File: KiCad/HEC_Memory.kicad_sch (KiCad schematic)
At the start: 10 parts, among them U13 74LS245, U14 74LS245, U15 74LS32, U16 74LS32, U2 AS6C4008-55PCN, U22 74LS02, U3 AS6C4008-55PCN, U4 CY7C199, U5 CY7C199, U9 74LS574

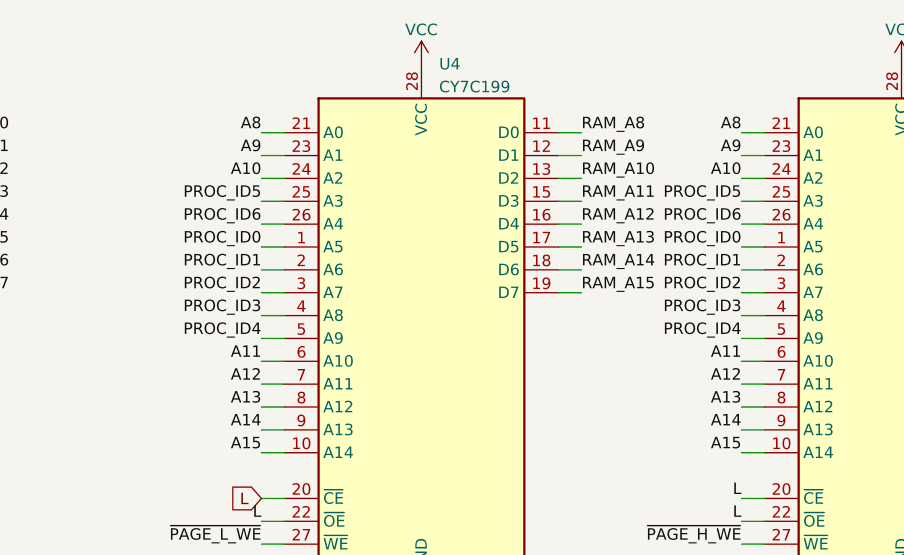
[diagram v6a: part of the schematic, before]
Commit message: More routing
Even more routing... Maybe 50% finished? The remaining 50% is probably harder though.
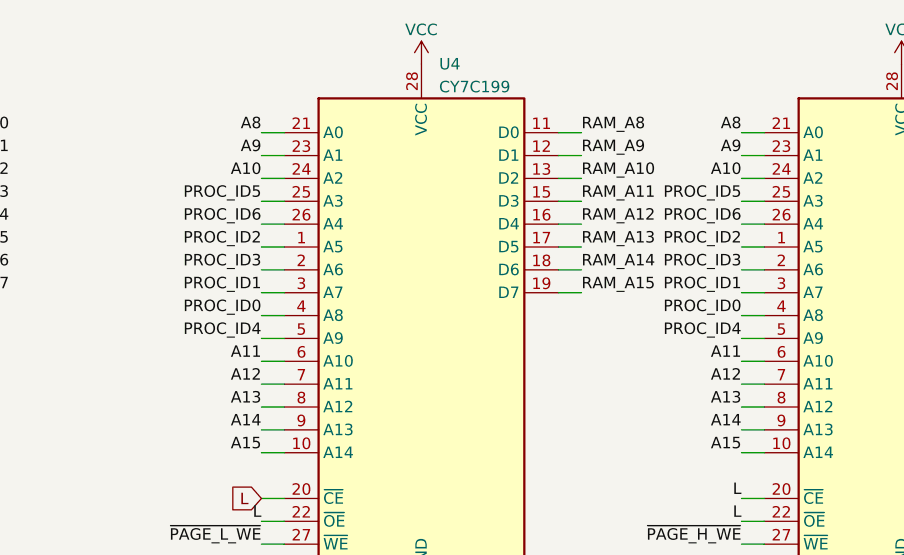
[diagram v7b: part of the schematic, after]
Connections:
- net PROC_ID0: now also U4.4 (A8), U5.4 (A8); no longer U4.1 (A5), U5.1 (A5)
- net PROC_ID1: now also U4.3 (A7), U5.3 (A7); no longer U4.2 (A6), U5.2 (A6)
- net PROC_ID2: now also U4.1 (A5), U5.1 (A5); no longer U4.3 (A7), U5.3 (A7)
- net PROC_ID3: now also U4.2 (A6), U5.2 (A6); no longer U4.4 (A8), U5.4 (A8)

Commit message: Livestream commit
Committing live! Just to make sure that I don't lose 1 day of work.
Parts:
- added U41: 74LS02, Package_DIP:DIP-14_W7.62mm_Socket, symbol 74xx:74LS02
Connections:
- net GND: now also U41.8
- net RAM_A19: now also U41.9; no longer U22.2, U22.3
- net VCC: now also U22.2, U22.3
- net ~{RAM_A19}: now also U41.10; no longer U22.1
- no-connect marks 0 -> 1
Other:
- moved on the sheet: U22A
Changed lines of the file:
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@@
 (kicad_sch (version 20230121) (generator eeschema)
   (paper "A4")
-  (junction (at 104.14 87.63) (diameter 0) (color 0 0 0 0)
-  )
+  (junction (at 69.215 86.36) (diameter 0) (color 0 0 0 0)
+  )
+  (no_connect (at 84.455 88.9))
   (wire (pts (xy 269.24 35.56) (xy 271.78 35.56))
     (stroke (width 0) (type default))
@@
     (stroke (width 0) (type default))
   )
-  (wire (pts (xy 104.14 85.09) (xy 104.14 87.63))
-    (stroke (width 0) (type default))
-  )
   (wire (pts (xy 269.875 33.02) (xy 269.24 33.02))
     (stroke (width 0) (type default))
@@
     (stroke (width 0) (type default))
   )
+  (wire (pts (xy 69.215 86.36) (xy 69.215 91.44))
+    (stroke (width 0) (type default))
+  )
   (wire (pts (xy 168.91 107.95) (xy 171.45 107.95))
     (stroke (width 0) (type default))
@@
     (stroke (width 0) (type default))
   )
+  (wire (pts (xy 92.075 85.09) (xy 104.14 85.09))
+    (stroke (width 0) (type default))
+  )
   (wire (pts (xy 190.5 158.115) (xy 190.5 148.59))
     (stroke (width 0) (type default))
@@
     (stroke (width 0) (type default))
   )
-  (wire (pts (xy 104.14 87.63) (xy 104.14 90.17))
-    (stroke (width 0) (type default))
-  )
   (wire (pts (xy 218.44 38.1) (xy 215.9 38.1))
     (stroke (width 0) (type default))
@@
     (stroke (width 0) (type default))
   )
+  (wire (pts (xy 69.215 82.55) (xy 69.215 86.36))
+    (stroke (width 0) (type default))
+  )
   (wire (pts (xy 50.8 167.64) (xy 53.34 167.64))
     (stroke (width 0) (type default))
@@
     (stroke (width 0) (type default))
   )
+  (wire (pts (xy 92.075 85.09) (xy 92.075 93.98))
+    (stroke (width 0) (type default))
+  )
   (wire (pts (xy 168.91 93.98) (xy 171.45 93.98))
     (stroke (width 0) (type default))
@@
     (stroke (width 0) (type default))
   )
-  (wire (pts (xy 101.6 87.63) (xy 104.14 87.63))
+  (wire (pts (xy 101.6 90.17) (xy 104.14 90.17))
     (stroke (width 0) (type default))
   )
@@
     (effects (font (size 1.27 1.27)) (justify left bottom))
   )
-  (label "RAM_A19" (at 101.6 87.63 180) (fields_autoplaced)
+  (label "RAM_A19" (at 101.6 90.17 180) (fields_autoplaced)
     (effects (font (size 1.27 1.27)) (justify right bottom))
   )
@@
         (path "/87935374-b60a-4f41-99da-94b76103dd77/933a6f90-eb98-4eb1-8c19-8a76228aece1"
           (reference "#PWR011") (unit 1)
+        )
+      )
+    )
+  )
+  (symbol (lib_id "power:VCC") (at 69.215 82.55 0) (unit 1)
+    (in_bom yes) (on_board yes) (dnp no) (fields_autoplaced)
+    (property "Reference" "#PWR0107" (at 69.215 86.36 0)
+      (effects (font (size 1.27 1.27)) hide)
+    )
+    (property "Value" "VCC" (at 69.215 79.375 0)
+      (effects (font (size 1.27 1.27)))
+    )
+    (property "Footprint" "" (at 69.215 82.55 0)
+      (effects (font (size 1.27 1.27)) hide)
+    )
+    (property "Datasheet" "" (at 69.215 82.55 0)
+      (effects (font (size 1.27 1.27)) hide)
+    )
+    (pin "1")
+    (instances
+      (project "HEC1"
+        (path "/87935374-b60a-4f41-99da-94b76103dd77/933a6f90-eb98-4eb1-8c19-8a76228aece1"
+          (reference "#PWR0107") (unit 1)
         )
       )
@@
     )
   )
+  (symbol (lib_id "power:GND") (at 92.075 93.98 0) (unit 1)
+    (in_bom yes) (on_board yes) (dnp no)
+    (property "Reference" "#PWR0107" (at 92.075 100.33 0)
+      (effects (font (size 1.27 1.27)) hide)
+    )
+    (property "Value" "GND" (at 92.075 99.06 0)
+      (effects (font (size 1.27 1.27)))
+    )
+    (property "Footprint" "" (at 92.075 93.98 0)
+      (effects (font (size 1.27 1.27)) hide)
+    )
+    (property "Datasheet" "" (at 92.075 93.98 0)
+      (effects (font (size 1.27 1.27)) hide)
+    )
+    (pin "1")
+    (instances
+      (project "HEC1"
+        (path "/87935374-b60a-4f41-99da-94b76103dd77"
+          (reference "#PWR0107") (unit 1)
+        )
+        (path "/87935374-b60a-4f41-99da-94b76103dd77/933a6f90-eb98-4eb1-8c19-8a76228aece1"
+          (reference "#PWR0134") (unit 1)
+        )
+      )
+    )
+  )
   (symbol (lib_id "power:GND") (at 250.19 151.13 0) (unit 1)
     (in_bom yes) (on_board yes) (dnp no) (fields_autoplaced)
@@
     )
   )
-  (symbol (lib_id "74xx:74LS02") (at 111.76 87.63 0) (unit 1)
-    (in_bom yes) (on_board yes) (dnp no) (fields_autoplaced)
-    (property "Reference" "U22" (at 111.76 79.375 0)
-      (effects (font (size 1.27 1.27)))
-    )
-    (property "Value" "74LS02" (at 111.76 81.915 0)
-      (effects (font (size 1.27 1.27)))
-    )
-    (property "Footprint" "Package_DIP:DIP-14_W7.62mm_Socket" (at 111.76 87.63 0)
-      (effects (font (size 1.27 1.27)) hide)
-    )
-    (property "Datasheet" "http://www.ti.com/lit/gpn/sn74ls02" (at 111.76 87.63 0)
+  (symbol (lib_id "74xx:74LS02") (at 76.835 88.9 0) (unit 1)
+    (in_bom yes) (on_board yes) (dnp no) (fields_autoplaced)
+    (property "Reference" "U22" (at 76.835 80.645 0)
+      (effects (font (size 1.27 1.27)))
+    )
+    (property "Value" "74LS02" (at 76.835 83.185 0)
+      (effects (font (size 1.27 1.27)))
+    )
+    (property "Footprint" "Package_DIP:DIP-14_W7.62mm_Socket" (at 76.835 88.9 0)
+      (effects (font (size 1.27 1.27)) hide)
+    )
+    (property "Datasheet" "http://www.ti.com/lit/gpn/sn74ls02" (at 76.835 88.9 0)
       (effects (font (size 1.27 1.27)) hide)
     )
@@
         )
       )
+    )
+  )
+  (symbol (lib_id "74xx:74LS02") (at 111.76 87.63 0) (unit 3)
+    (in_bom yes) (on_board yes) (dnp no) (fields_autoplaced)
+    (property "Reference" "U41" (at 111.76 79.375 0)
+      (effects (font (size 1.27 1.27)))
+    )
+    (property "Value" "74LS02" (at 111.76 81.915 0)
+      (effects (font (size 1.27 1.27)))
+    )
+    (property "Footprint" "Package_DIP:DIP-14_W7.62mm_Socket" (at 111.76 87.63 0)
+      (effects (font (size 1.27 1.27)) hide)
+    )
+    (property "Datasheet" "http://www.ti.com/lit/gpn/sn74ls02" (at 111.76 87.63 0)
+      (effects (font (size 1.27 1.27)) hide)
+    )
+    (pin "1")
+    (pin "2")
+    (pin "3")
+    (pin "4")
+    (pin "5")
+    (pin "6")
+    (pin "10")
+    (pin "8")
+    (pin "9")
+    (pin "11")
+    (pin "12")
+    (pin "13")
+    (pin "14")
+    (pin "7")
+    (instances
+      (project "HEC1"
+        (path "/87935374-b60a-4f41-99da-94b76103dd77/2930b625-d6a3-4a7f-9d41-a454efcef99d"
+          (reference "U41") (unit 3)
+        )
+        (path "/87935374-b60a-4f41-99da-94b76103dd77"
+          (reference "U41") (unit 3)
+        )
+        (path "/87935374-b60a-4f41-99da-94b76103dd77/933a6f90-eb98-4eb1-8c19-8a76228aece1"
+          (reference "U41") (unit 3)
+        )
+      )
